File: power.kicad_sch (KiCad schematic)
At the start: 128 parts, among them Q2 BC817-25W, Q3 DZDH0401DW, Q4 DZDH0401DW, Q5 SI7613DN-T1-GE3, Q6 SI7613DN-T1-GE3, U1 LT8350RV#PBF, U2 MP2386GG, U3 TPS65983BAZBHR

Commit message: [#58582] Globlib
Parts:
- removed R98, R99: R_0R_22.4A_0603, thunderbolt-pcie-adapter-footprints:R_0603_1608Metric, symbol thunderbolt-pcie-adapter:R_0R_22.4A_0603
- C10, C13, C15, C17, C8: footprint thunderbolt-pcie-adapter-footprints:C_1206_3216Metric -> antmicro-footprints:C_1206_3216Metric; symbol thunderbolt-pcie-adapter:C_22u_1206_35V -> antmicroCapacitorsmisc:C_22u_1206_35V
- C11, C12, C7, C9: footprint thunderbolt-pcie-adapter-footprints:C_0805_2012Metric -> antmicro-footprints:C_0805_2012Metric; symbol thunderbolt-pcie-adapter:C_10u_0805_35V -> antmicroCapacitorsmisc:C_10u_0805_35V
- C119, C122, C38, C40, C43, C46, C50: footprint thunderbolt-pcie-adapter-footprints:C_0603_1608Metric -> antmicro-footprints:C_0603_1608Metric; symbol thunderbolt-pcie-adapter:C_22u_16V_0603 -> antmicroCapacitors0603:C_22u_16V_0603
- C14, C24, C26, C28, C29, C32: footprint thunderbolt-pcie-adapter-footprints:C_0402_1005Metric -> antmicro-footprints:C_0402_1005Metric; symbol thunderbolt-pcie-adapter:C_100n_0402 -> antmicroCapacitors0402:C_100n_0402
- C16, C27, C31: footprint thunderbolt-pcie-adapter-footprints:C_0402_1005Metric -> antmicro-footprints:C_0402_1005Metric; symbol thunderbolt-pcie-adapter:C_220n_0402 -> antmicroCapacitors0402:C_220n_0402
- C18, C22, C25, C34: footprint thunderbolt-pcie-adapter-footprints:C_0402_1005Metric -> antmicro-footprints:C_0402_1005Metric; symbol thunderbolt-pcie-adapter:C_1u_0402 -> antmicroCapacitors0402:C_1u_0402
- C19: footprint thunderbolt-pcie-adapter-footprints:C_0402_1005Metric -> antmicro-footprints:C_0402_1005Metric; symbol thunderbolt-pcie-adapter:C_22n_0402 -> antmicroCapacitors0402:C_22n_0402
- C20, C21: footprint thunderbolt-pcie-adapter-footprints:C_0402_1005Metric -> antmicro-footprints:C_0402_1005Metric; symbol thunderbolt-pcie-adapter:C_4u7_25V_0402 -> antmicroCapacitors0402:C_4u7_25V_0402
- C23, C39: footprint thunderbolt-pcie-adapter-footprints:C_0402_1005Metric -> antmicro-footprints:C_0402_1005Metric; symbol thunderbolt-pcie-adapter:C_10u_0402 -> antmicroCapacitors0402:C_10u_0402
- C30: footprint thunderbolt-pcie-adapter-footprints:C_0402_1005Metric -> antmicro-footprints:C_0402_1005Metric; symbol thunderbolt-pcie-adapter:C_4n7_0402 -> antmicroCapacitors0402:C_4n7_0402
- C33: footprint thunderbolt-pcie-adapter-footprints:C_0402_1005Metric -> antmicro-footprints:C_0402_1005Metric; symbol thunderbolt-pcie-adapter:C_33p_0402 -> antmicroCapacitors0402:C_33p_0402
- C35, C36, C37: footprint thunderbolt-pcie-adapter-footprints:C_0402_1005Metric -> antmicro-footprints:C_0402_1005Metric; symbol thunderbolt-pcie-adapter:C_2u2_0402 -> antmicroCapacitors0402:C_2u2_0402
- C41, C44, C47: footprint thunderbolt-pcie-adapter-footprints:C_0603_1608Metric -> antmicro-footprints:C_0603_1608Metric; symbol thunderbolt-pcie-adapter:C_22u_0603 -> antmicroCapacitors0603:C_22u_0603
- C42, C48: footprint thunderbolt-pcie-adapter-footprints:C_0805_2012Metric -> antmicro-footprints:C_0805_2012Metric; symbol thunderbolt-pcie-adapter:C_22u_25V_0805 -> antmicroCapacitorsmisc:C_22u_25V_0805
- C45, C49: footprint thunderbolt-pcie-adapter-footprints:C_0402_1005Metric -> antmicro-footprints:C_0402_1005Metric; symbol thunderbolt-pcie-adapter:C_220p_0402 -> antmicroCapacitors0402:C_220p_0402
- D1: footprint thunderbolt-pcie-adapter-footprints:D_SOD-323F -> antmicro-footprints:D_SOD-323F; symbol thunderbolt-pcie-adapter:MM3Z3V3C -> antmicroDiodesZenerSingle:MM3Z3V3C
- D2, D3, D5: footprint thunderbolt-pcie-adapter-footprints:LED_0603_1608Metric_G -> antmicro-footprints:LED_0603_1608Metric_G; symbol thunderbolt-pcie-adapter:LED_G_0603_KP-1608CGCK -> antmicroLEDIndicationDiscrete:LED_G_0603_KP-1608CGCK
- FB1, FB2, FB3: footprint thunderbolt-pcie-adapter-footprints:FB_0805_2012Metric -> antmicro-footprints:FB_0805_2012Metric; symbol thunderbolt-pcie-adapter:BLM21SN300SZ1D -> antmicroFerriteBeadsandChips:FB_30Z_8.5A_Murata-BLM21SN_0805
- L1: footprint thunderbolt-pcie-adapter-footprints:L_Coilcraft_XAL7070 -> antmicro-footprints:L_Coilcraft-XAL7070; symbol thunderbolt-pcie-adapter:L_6u8_12.8A_XAL7070 -> antmicroFixedInductors:L_6u8_12.8A_Coilcraft-XAL7070
- L2: footprint thunderbolt-pcie-adapter-footprints:L_Coilcraft_XAL5030 -> antmicro-footprints:L_Coilcraft-XAL5030; symbol thunderbolt-pcie-adapter:L_2u2_10.4A_XAL5030 -> antmicroFixedInductors:L_2u2_9.7A_Coilcraft-XAL5030
- Q2: footprint thunderbolt-pcie-adapter-footprints:SOT-323 -> antmicro-footprints:SOT-323; symbol thunderbolt-pcie-adapter:BC817-25W -> antmicroTransistorsBipolarSingle:BC817-25W
- Q3, Q4: footprint thunderbolt-pcie-adapter-footprints:SOT-363 -> antmicro-footprints:SOT-363; symbol thunderbolt-pcie-adapter:DZDH0401DW -> antmicroPMICORControllersIdealDiodes:DZDH0401DW
- Q5, Q6: footprint thunderbolt-pcie-adapter-footprints:Vishay_PowerPAK_1212-8_Single -> antmicro-footprints:Vishay_PowerPAK_1212-8_Single; symbol thunderbolt-pcie-adapter:SI7613DN-T1-GE3 -> antmicroTransistorsFETsMOSFETsSingle:SI7613DN-T1-GE3
- R10, R22, R23, R24, R29, R30, R33, R34, R4, R9, R92, R95, R96: footprint thunderbolt-pcie-adapter-footprints:R_0402_1005Metric -> antmicro-footprints:R_0402_1005Metric; symbol thunderbolt-pcie-adapter:R_100k_0402 -> antmicroResistors0402:R_100k_0402
- R11, R16, R17, R19, R2, R20, R32, R39, R44, R6, R8, R91, R93, R94: footprint thunderbolt-pcie-adapter-footprints:R_0402_1005Metric -> antmicro-footprints:R_0402_1005Metric; symbol thunderbolt-pcie-adapter:R_10k_0402 -> antmicroResistors0402:R_10k_0402
- R12, R13, R18, R26, R27, R31: footprint thunderbolt-pcie-adapter-footprints:R_0402_1005Metric -> antmicro-footprints:R_0402_1005Metric; symbol thunderbolt-pcie-adapter:R_0R_0402 -> antmicroResistors0402:R_0R_0402
- R14, R15: footprint thunderbolt-pcie-adapter-footprints:R_0402_1005Metric -> antmicro-footprints:R_0402_1005Metric; symbol thunderbolt-pcie-adapter:R_3k3_0402 -> antmicroResistors0402:R_3k3_0402
- R21: footprint thunderbolt-pcie-adapter-footprints:R_0402_1005Metric -> antmicro-footprints:R_0402_1005Metric; symbol thunderbolt-pcie-adapter:R_1M_0402 -> antmicroResistors0402:R_1M_0402
- R25: footprint thunderbolt-pcie-adapter-footprints:R_0402_1005Metric -> antmicro-footprints:R_0402_1005Metric; symbol thunderbolt-pcie-adapter:R_12k_0402 -> antmicroResistors0402:R_12k_0402
- R28: footprint thunderbolt-pcie-adapter-footprints:R_0402_1005Metric -> antmicro-footprints:R_0402_1005Metric; symbol thunderbolt-pcie-adapter:R_124k_0402 -> antmicroResistors0402:R_124k_0402
- R3, R46, R5, R97: footprint thunderbolt-pcie-adapter-footprints:R_0402_1005Metric -> antmicro-footprints:R_0402_1005Metric; symbol thunderbolt-pcie-adapter:R_2k2_0402 -> antmicroResistors0402:R_2k2_0402
- R35: footprint thunderbolt-pcie-adapter-footprints:R_0402_1005Metric -> antmicro-footprints:R_0402_1005Metric; symbol thunderbolt-pcie-adapter:R_15k_0.1%_0402 -> antmicroResistors0402:R_15k_0.1%_0402
- R36: footprint thunderbolt-pcie-adapter-footprints:R_0402_1005Metric -> antmicro-footprints:R_0402_1005Metric; symbol thunderbolt-pcie-adapter:R_40k2_0402 -> antmicroResistors0402:R_40k2_0402
- R37: footprint thunderbolt-pcie-adapter-footprints:R_0402_1005Metric -> antmicro-footprints:R_0402_1005Metric; symbol thunderbolt-pcie-adapter:R_8k87_0402 -> antmicroResistors0402:R_8k87_0402
- R38, R40: footprint thunderbolt-pcie-adapter-footprints:R_0402_1005Metric -> antmicro-footprints:R_0402_1005Metric; symbol thunderbolt-pcie-adapter:R_5k1_0402 -> antmicroResistors0402:R_5k1_0402
- R41: footprint thunderbolt-pcie-adapter-footprints:R_0603_1608Metric -> antmicro-footprints:R_0603_1608Metric; symbol thunderbolt-pcie-adapter:R_0R_0603 -> antmicroResistors0603:R_0R_0603
- R42: footprint thunderbolt-pcie-adapter-footprints:R_0402_1005Metric -> antmicro-footprints:R_0402_1005Metric; symbol thunderbolt-pcie-adapter:R_330R_0402 -> antmicroResistors0402:R_330R_0402
- R43: footprint thunderbolt-pcie-adapter-footprints:R_0402_1005Metric -> antmicro-footprints:R_0402_1005Metric; symbol thunderbolt-pcie-adapter:R_110k_0402 -> antmicroResistors0402:R_110k_0402
- R45: footprint thunderbolt-pcie-adapter-footprints:R_1206_3216Metric -> antmicro-footprints:R_1206_3216Metric; symbol thunderbolt-pcie-adapter:R_0R02_1206 -> antmicroResistorsmisc:R_0R02_1206
- R7: footprint thunderbolt-pcie-adapter-footprints:R_0402_1005Metric -> antmicro-footprints:R_0402_1005Metric; symbol thunderbolt-pcie-adapter:R_24k_0402 -> antmicroResistors0402:R_24k_0402
- TP1, TP12, TP2, TP3, TP5, TP7, TP8: footprint thunderbolt-pcie-adapter-footprints:Testpoint_smd_1mm -> antmicro-footprints:TP_SMD_1mm; symbol thunderbolt-pcie-adapter:TP_1mm_SMD -> antmicroTestPoints:TP_1mm_SMD
- TP4, TP6: footprint thunderbolt-pcie-adapter-footprints:TP_SMD_0.75mm -> antmicro-footprints:TP_SMD_0.75mm; symbol thunderbolt-pcie-adapter:TP_0.75mm_SMD -> antmicroTestPoints:TP_0.75mm_SMD
- U1: footprint thunderbolt-pcie-adapter-footprints:LT8350 -> antmicro-footprints:QFN-32-4EP_4x6mm_P0.5mm; symbol thunderbolt-pcie-adapter:LT8350RV#PBF -> antmicroDCDCConverters:LT8350RV
- U2: footprint thunderbolt-pcie-adapter-footprints:QFN-11_2x2mm_P0.5mm -> antmicro-footprints:QFN-11_2x2mm_P0.5mm; symbol thunderbolt-pcie-adapter:MP2386GG -> antmicroDCDCConverters:MP2386GG
- U3: footprint thunderbolt-pcie-adapter-footprints:IC_TPS65983BAZBHR -> antmicro-footprints:IC_TPS65983BAZBHR; symbol thunderbolt-pcie-adapter:TPS65983BAZBHR -> antmicroInterfaceControllers:TPS65983BAZBHR
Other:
- note added: "R98 0R 22.4A PMR03EZPJ000"
- note added: "R99 0R 22.4A PMR03EZPJ000"

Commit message: [#58582] WiP: Update symbols to global
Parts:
- C10, C13, C15, C17, C8: Val 22u/35V -> 22u; Voltage (none) -> 35V
- C11, C12, C7, C9: Val 10u/35V -> 10u; Voltage (none) -> 35V
- C119, C122, C38, C40, C43, C46, C50: Manufacturer Samsung -> Samsung Electro-Mechanics; Val 22u/16V -> 22u; Voltage (none) -> 16V
- C16, C23, C39: Manufacturer Yaego -> YAGEO
- C33: MPN MC0402N330J500CT -> 04025A330FAT2A; Manufacturer Multicomp -> KYOCERA AVX
- C42, C48: Dielectric (none) -> X5R; Manufacturer Samsung -> Samsung Electro-Mechanics; Val 22u_25V -> 22u; Voltage (none) -> 25V
- C45, C49: MPN MC0402B221K500CT -> 04025C221JAT2A; Manufacturer Multicomp -> KYOCERA AVX
- D2, D3, D5: Color (none) -> Green
- FB1, FB2, FB3: value BLM21SN300SZ1D -> FB_30Z_8.5A_Murata-BLM21SN_0805; Val (none) -> 30Z/8.5A
- L1: value L_6u8_12.8A_XAL7070 -> L_6u8_12.8A_Coilcraft-XAL7070; IMax 9.2 -> 9.2 A; ISat 12.8 -> 12.8 A
- L2: value L_2u2_10.4A_XAL5030 -> L_2u2_9.7A_Coilcraft-XAL5030; IMax 9.7 -> 9.7 A; ISat 9.2 -> 9.2 A; Val 2u2/10.4A -> 2u2/9.7A
- Q3: MPN DZDH0401DW-7 -> DZDH0401DW
- R24: DNP DNP -> (none)
- R45: MPN WSLP1206R0200FEA -> WSLP1206R0200FEA
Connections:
- net 12V0_DCDC: now also D3.2 (A); no longer D3.1
- net 12V0_MOLEX: now also D5.2 (A); no longer D5.1
- net GND: now also D1.1 (C); no longer D1.A
- net at R11.2, R6.1, U2.11 (EN): now also D1.2 (A); no longer D1.K
- net at C33.2, C41.2, C44.2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: now also D2.2 (A); no longer D2.1
- net at R46.2: now also D3.1 (C); no longer D3.2
- net at R97.2: now also D5.1 (C); no longer D5.2
- net at R42.2: now also D2.1 (C); no longer D2.2
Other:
- moved on the sheet: C34, C35, C36, C37, D1, D2, D3, D5

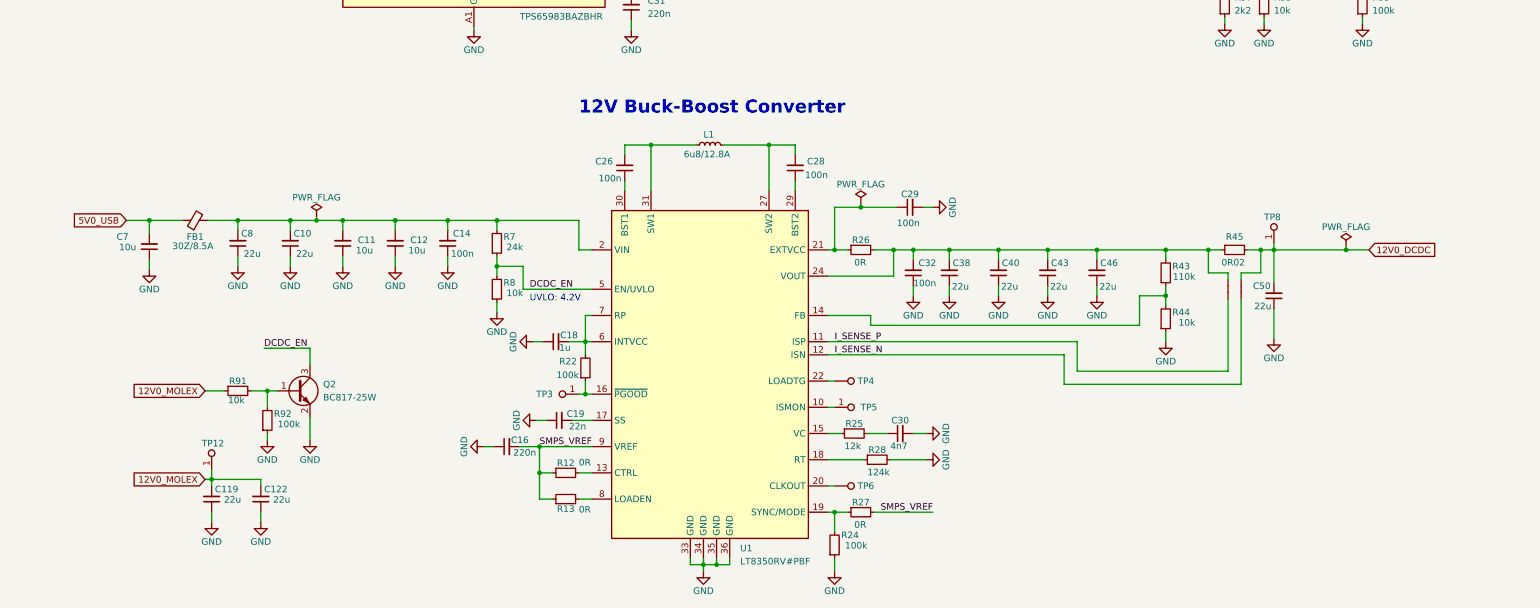
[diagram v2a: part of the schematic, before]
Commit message: [#58582] Update U1 to global lib
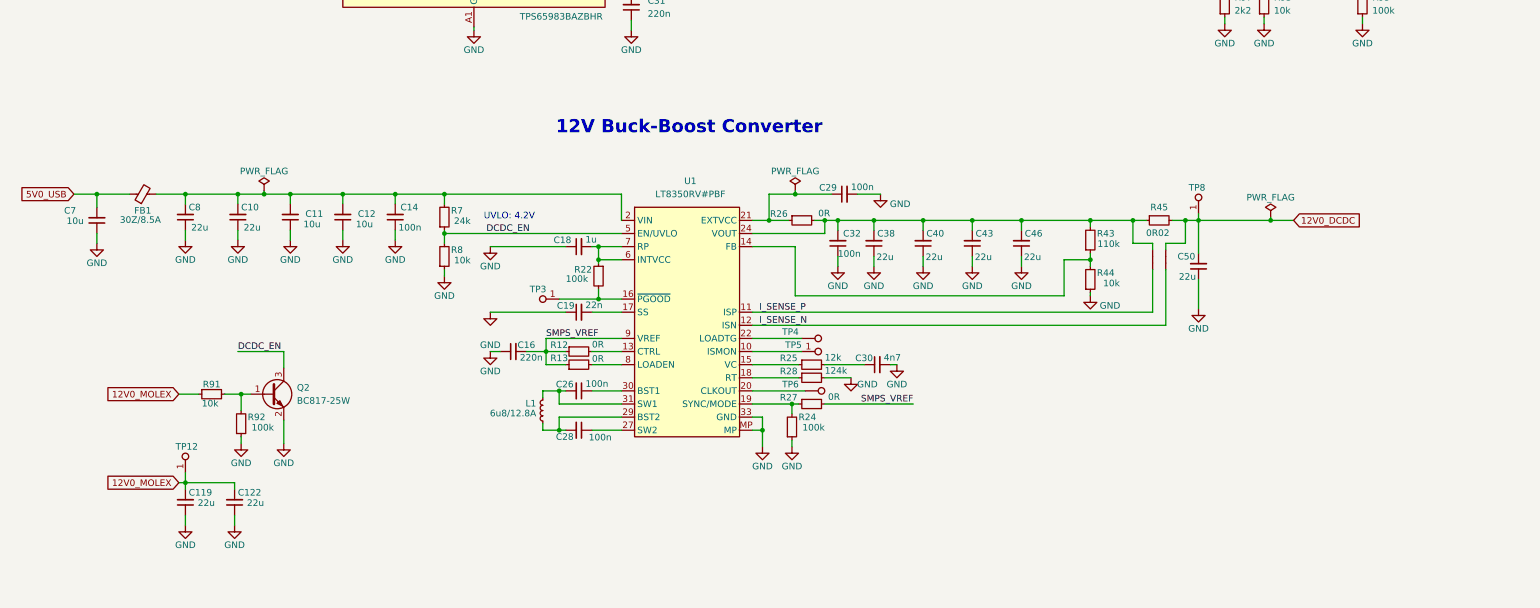
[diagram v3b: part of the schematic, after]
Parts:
- U1: value LT8350RV#PBF -> LT8350RV
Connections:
- net GND: now also U1.MP
- net at TP3.1, U1.16 (~{PGOOD}): now also R22.2; no longer R22.1
- net at C18.2, U1.6 (INTVCC), U1.7 (RP): now also R22.1; no longer R22.2
- net at U1.27 (SW2), U1.28 (SW2): now also C28.1; no longer C28.2, L1.2
- net at U1.29 (BST2): now also C28.2, L1.2; no longer C28.1
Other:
- moved on the sheet: C10, C11, C119, C12, C122, C14, C16, C18, C19, C26, C28, C29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

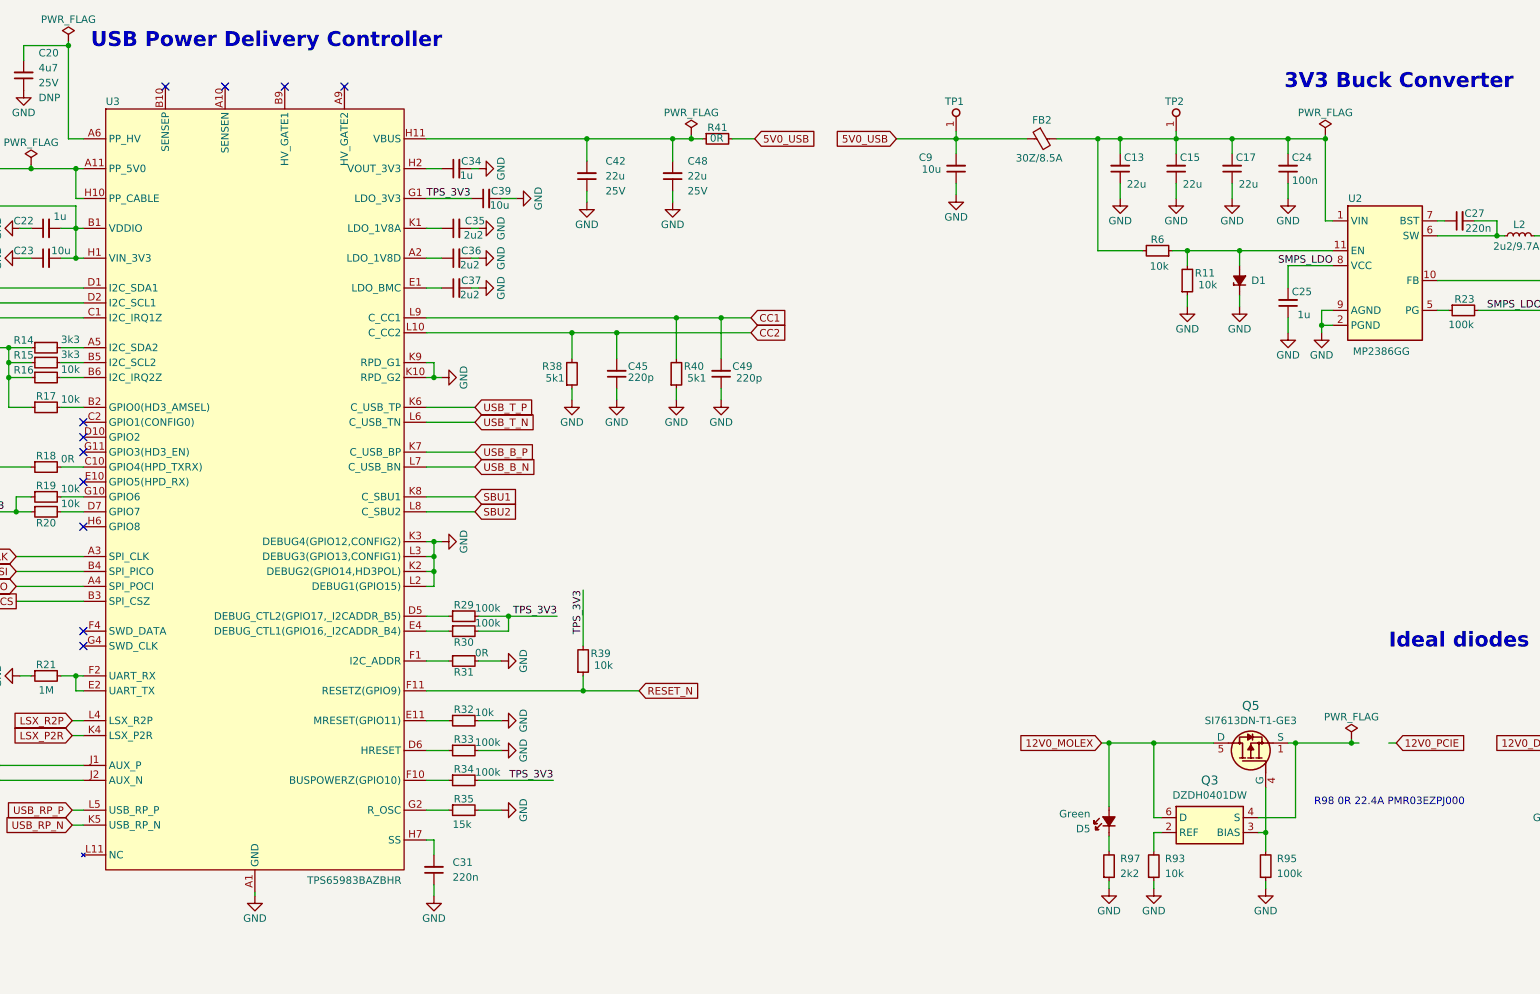
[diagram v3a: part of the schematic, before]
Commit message: [#58582] Update ICs to global libs
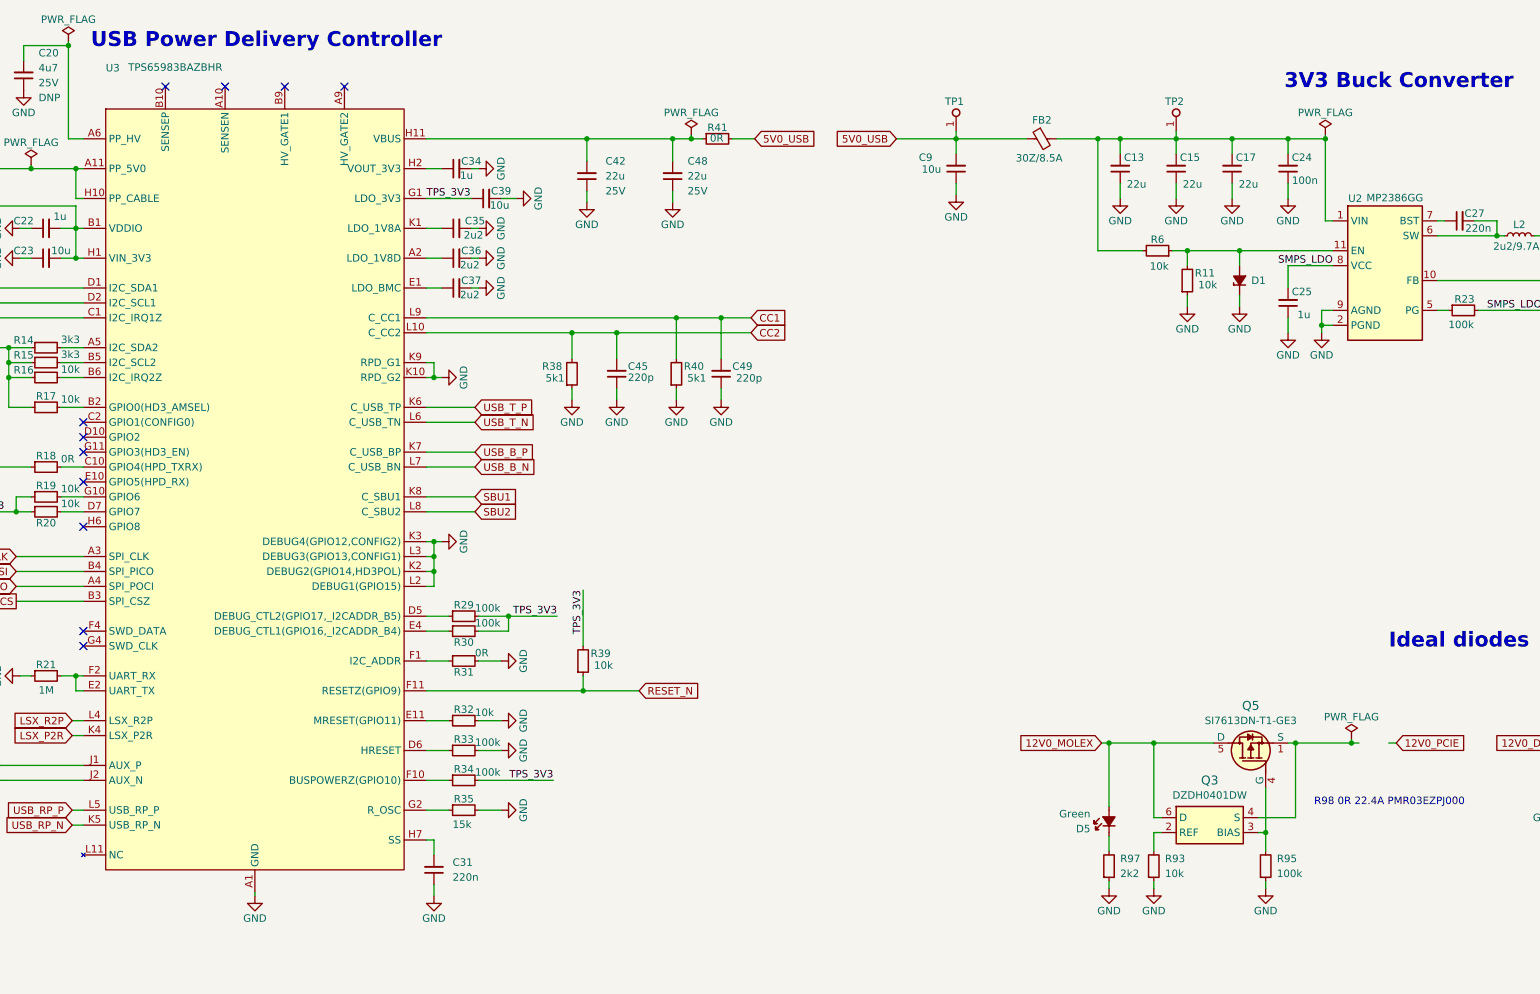
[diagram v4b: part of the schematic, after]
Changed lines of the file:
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@@
       (effects (font (size 1.27 1.27) (thickness 0.15)))
     )
-    (property "Value" "MP2386GG" (at 297.18 79.375 0)
-      (effects (font (size 1.27 1.27) (thickness 0.15)))
+    (property "Value" "MP2386GG" (at 294.64 53.975 0)
+      (effects (font (size 1.27 1.27) (thickness 0.15)) (justify left bottom))
     )
     (property "Footprint" "antmicro-footprints:QFN-11_2x2mm_P0.5mm" (at 321.945 67.31 0)
@@
   (symbol (lib_id "antmicroInterfaceControllers:TPS65983BAZBHR") (at 76.2 43.18 0) (unit 1)
     (in_bom yes) (on_board yes) (dnp no)
-    (property "Reference" "U3" (at 80.01 36.83 0)
+    (property "Reference" "U3" (at 80.01 31.115 0)
       (effects (font (size 1.27 1.27) (thickness 0.15)) (justify left))
     )
-    (property "Value" "TPS65983BAZBHR" (at 114.3 170.18 0)
+    (property "Value" "TPS65983BAZBHR" (at 83.82 31.75 0)
       (effects (font (size 1.27 1.27) (thickness 0.15)) (justify left bottom))
     )

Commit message: [#58582] Update GND to global
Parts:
- added R98, R99: R_0R_22.4A_0603, antmicro-footprints:R_0603_1608Metric, symbol antmicroResistors0603:R_0R_22.4A_0603
- TP1, TP12, TP2, TP3, TP5, TP7, TP8: now left out of the parts list
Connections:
- net 12V0_PCIE: now also R98.2, R99.2
- net at Q3.4 (S), Q5.1 (S), Q5.2 (S)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: now also R98.1
- net at Q4.4 (S), Q6.1 (S), Q6.2 (S)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: now also R99.1
